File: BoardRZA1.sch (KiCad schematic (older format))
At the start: 151 parts, among them CON1 USB-MINI-B, CON2 USB-MINI-B, CON3 con-microSD, CON4 BARREL_JACK, J1 HR911105A, J2 SIL38, P1 CONN_5X2, SW1 RESET, SW2 NMI, SW3 SW0, SW4 SW1, U1 RZ-A1L, U2 OSC_4PIN, U3 OSC_4PIN, U4 N25QXXX, U5 AS4C16M16S, U6 BA3259HFP, U7 BU42xx, U8 KSZ8041MLL, X1 32.768k, X2 20MHz

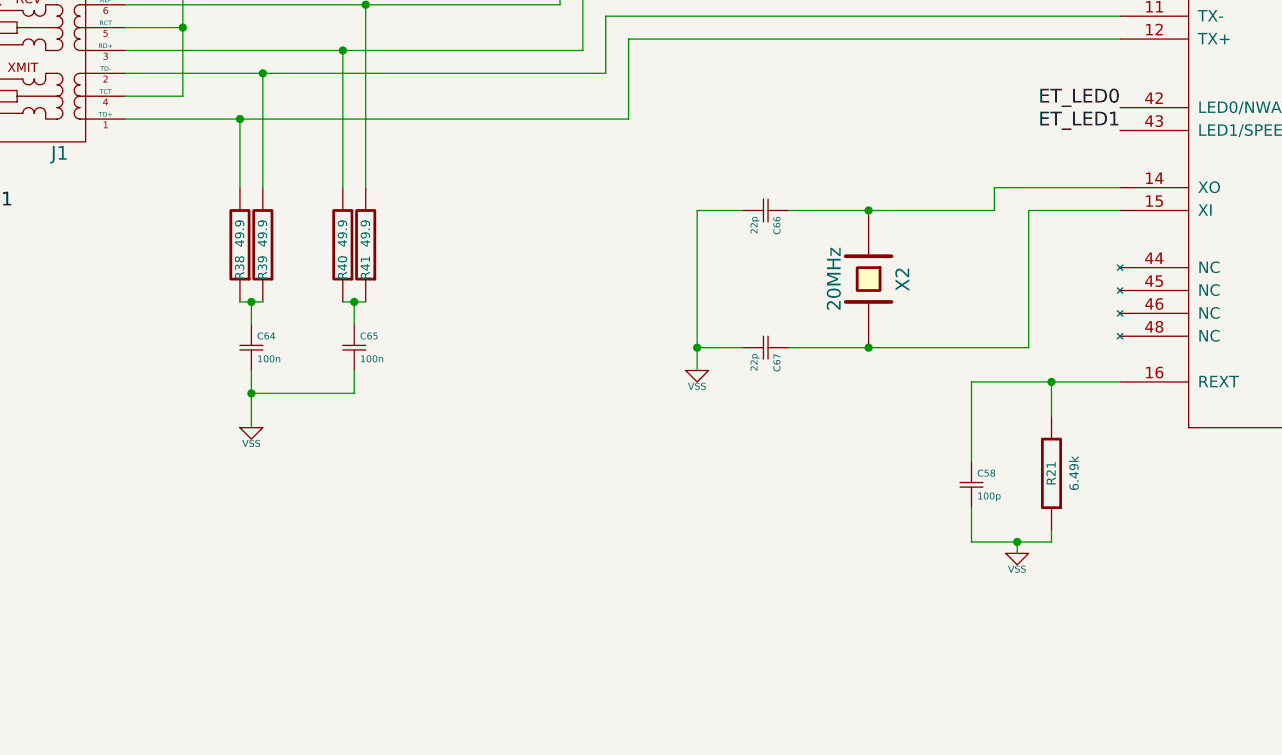
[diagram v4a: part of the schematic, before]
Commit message: Cambia XTAL 25MHz Phy por OSC 25MHz
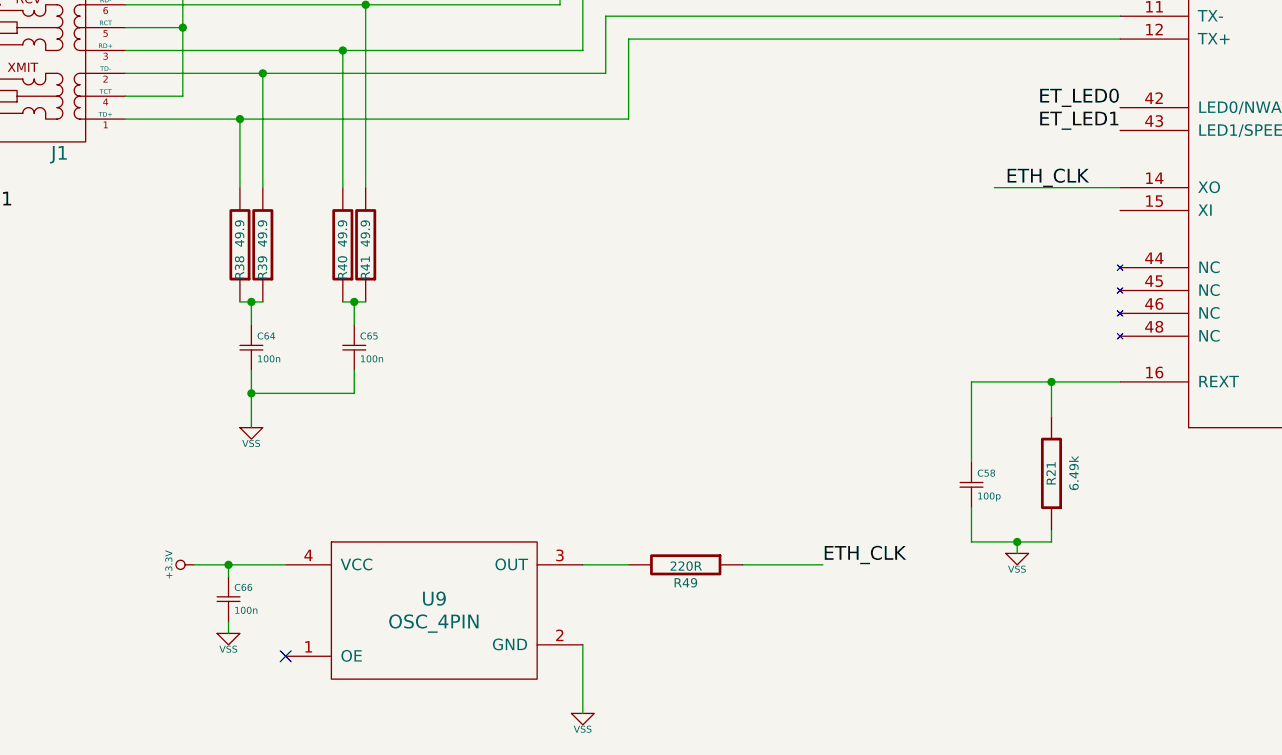
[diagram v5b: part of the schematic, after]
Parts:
- removed C67: 22p, SMD_Packages:SM0805, symbol Csmall
- removed X2: 20MHz, Crystals:Crystal_HC49-SD_SMD, symbol CRYSTAL
- added R49: 220R, SMD_Packages:SM0805, symbol R
- added U9: OSC_4PIN, OSC_4PIN:OSC_4PIN, symbol OSC_4PIN
- C66: value 22p -> 100n
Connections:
- net +3.3V: now also C66.1, U9.4 (VCC)
- net VSS: now also U9.2 (GND)
- net ETH_CLK: now reaches U8.14 (XO)
- net ETH_CLK: now also R49.1; no longer C66.1
- new net: R49.2, U9.3 (OUT)
- no-connect marks 13 -> 14
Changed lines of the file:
@@
 PHY_RESET
-$Comp
-L CRYSTAL X2
-U 1 1 5466F768
-P 22850 24400
-F 0 "X2" H 22850 24550 60  0000 C CNN
-F 1 "20MHz" H 22850 24250 60  0000 C CNN
-F 2 "Crystals:Crystal_HC49-SD_SMD" H 22850 24400 60  0001 C CNN
-F 3 "" H 22850 24400 60  0000 C CNN
-	1    22850 24400
-	0    1    1    0
-$EndComp
-$Comp
-L Csmall C67
-U 1 1 5466FA33
-P 22400 24700
-F 0 "C67" H 22425 24750 30  0000 L CNN
-F 1 "22p" H 22425 24650 30  0000 L CNN
-F 2 "SMD_Packages:SM0805" H 22400 24700 60  0001 C CNN
-F 3 "" H 22400 24700 60  0000 C CNN
-	1    22400 24700
-	0    1    1    0
-$EndComp
-$Comp
-L Csmall C66
-U 1 1 5466FE7E
-P 22400 24100
-F 0 "C66" H 22425 24150 30  0000 L CNN
-F 1 "22p" H 22425 24050 30  0000 L CNN
-F 2 "SMD_Packages:SM0805" H 22400 24100 60  0001 C CNN
-F 3 "" H 22400 24100 60  0000 C CNN
-	1    22400 24100
-	0    1    1    0
-$EndComp
-$Comp
-L VSS #PWR055
-U 1 1 54671C74
-P 22100 24800
-F 0 "#PWR055" H 22100 24800 30  0001 C CNN
-F 1 "VSS" H 22100 24730 30  0000 C CNN
-F 2 "" H 22100 24800 60  0000 C CNN
-F 3 "" H 22100 24800 60  0000 C CNN
-	1    22100 24800
-	1    0    0    -1
-$EndComp
 $Comp
 L INDUCTOR_SMALL L10
@@
 $EndComp
 $Comp
-L VSS #PWR056
+L VSS #PWR055
 U 1 1 5467CDAE
 P 20150 25050
-F 0 "#PWR056" H 20150 25050 30  0001 C CNN
+F 0 "#PWR055" H 20150 25050 30  0001 C CNN
 F 1 "VSS" H 20150 24980 30  0000 C CNN
 F 2 "" H 20150 25050 60  0000 C CNN
@@
 $EndComp
 $Comp
-L VSS #PWR057
+L VSS #PWR056
 U 1 1 5467DB95
 P 18250 24100
-F 0 "#PWR057" H 18250 24100 30  0001 C CNN
+F 0 "#PWR056" H 18250 24100 30  0001 C CNN
 F 1 "VSS" H 18250 24030 30  0000 C CNN
 F 2 "" H 18250 24100 60  0000 C CNN
@@
 $EndComp
 $Comp
-L VSS #PWR058
+L VSS #PWR057
 U 1 1 5467E4B1
 P 18050 22600
-F 0 "#PWR058" H 18050 22600 30  0001 C CNN
+F 0 "#PWR057" H 18050 22600 30  0001 C CNN
 F 1 "VSS" H 18050 22530 30  0000 C CNN
 F 2 "" H 18050 22600 60  0000 C CNN
@@
 $EndComp
 $Comp
-L VSS #PWR059
+L VSS #PWR058
 U 1 1 5467ECC7
 P 19950 23100
-F 0 "#PWR059" H 19950 23100 30  0001 C CNN
+F 0 "#PWR058" H 19950 23100 30  0001 C CNN
 F 1 "VSS" H 19950 23030 30  0000 C CNN
 F 2 "" H 19950 23100 60  0000 C CNN
@@
 $EndComp
 $Comp
-L +3.3V #PWR060
+L +3.3V #PWR059
 U 1 1 546866CA
 P 18600 21700
-F 0 "#PWR060" H 18600 21660 30  0001 C CNN
+F 0 "#PWR059" H 18600 21660 30  0001 C CNN
 F 1 "+3.3V" H 18600 21810 30  0000 C CNN
 F 2 "" H 18600 21700 60  0000 C CNN
@@
 	26250 22600 26850 22600
 Wire Wire Line
-	22500 24100 23400 24100
-Wire Wire Line
 	23950 24000 23400 24000
-Wire Wire Line
-	23400 24000 23400 24100
-Connection ~ 22850 24100
-Wire Wire Line
-	22500 24700 23550 24700
-Wire Wire Line
-	23550 24700 23550 24100
-Wire Wire Line
-	23550 24100 23950 24100
-Connection ~ 22850 24700
-Wire Wire Line
-	22300 24100 22100 24100
-Wire Wire Line
-	22100 24100 22100 24800
-Wire Wire Line
-	22100 24700 22300 24700
-Connection ~ 22100 24700
 Wire Wire Line
 	19600 23500 21700 23500
@@
 Connection ~ 18500 24100
 $Comp
-L VSS #PWR061
+L VSS #PWR060
 U 1 1 5468A27A
 P 18500 24750
-F 0 "#PWR061" H 18500 24750 30  0001 C CNN
+F 0 "#PWR060" H 18500 24750 30  0001 C CNN
 F 1 "VSS" H 18500 24680 30  0000 C CNN
 F 2 "" H 18500 24750 60  0000 C CNN
@@
 $EndComp
 $Comp
-L +3.3V #PWR062
+L +3.3V #PWR061
 U 1 1 5468A8E5
 P 18800 24650
-F 0 "#PWR062" H 18800 24610 30  0001 C CNN
+F 0 "#PWR061" H 18800 24610 30  0001 C CNN
 F 1 "+3.3V" H 18800 24760 30  0000 C CNN
 F 2 "" H 18800 24650 60  0000 C CNN
@@
 	18500 24650 18500 24750
 $Comp
-L VSS #PWR063
+L VSS #PWR062
 U 1 1 546806AB
 P 8350 12150
-F 0 "#PWR063" H 8350 12150 30  0001 C CNN
+F 0 "#PWR062" H 8350 12150 30  0001 C CNN
 F 1 "VSS" H 8350 12080 30  0000 C CNN
 F 2 "" H 8350 12150 60  0000 C CNN
@@
 	8350 11950 8100 11950
 $Comp
-L +3.3V #PWR064
+L +3.3V #PWR063
 U 1 1 54681794
 P 8200 8100
-F 0 "#PWR064" H 8200 8060 30  0001 C CNN
+F 0 "#PWR063" H 8200 8060 30  0001 C CNN
 F 1 "+3.3V" H 8200 8210 30  0000 C CNN
 F 2 "" H 8200 8100 60  0000 C CNN
@@
 $EndComp
 $Comp
-L +3.3V #PWR065
+L +3.3V #PWR064
 U 1 1 5468C052
 P 15250 3050
-F 0 "#PWR065" H 15250 3010 30  0001 C CNN
+F 0 "#PWR064" H 15250 3010 30  0001 C CNN
 F 1 "+3.3V" H 15250 3160 30  0000 C CNN
 F 2 "" H 15250 3050 60  0000 C CNN
@@
 $EndComp
 $Comp
-L +3.3V #PWR066
+L +3.3V #PWR065
 U 1 1 5468A3EB
 P 23550 2850
-F 0 "#PWR066" H 23550 2810 30  0001 C CNN
+F 0 "#PWR065" H 23550 2810 30  0001 C CNN
 F 1 "+3.3V" H 23550 2960 30  0000 C CNN
 F 2 "" H 23550 2850 60  0000 C CNN
@@
 	24150 2850 24400 2850
 $Comp
-L VSS #PWR067
+L VSS #PWR066
 U 1 1 5468ACC4
 P 25150 2850
-F 0 "#PWR067" H 25150 2850 30  0001 C CNN
+F 0 "#PWR066" H 25150 2850 30  0001 C CNN
 F 1 "VSS" H 25150 2780 30  0000 C CNN
 F 2 "" H 25150 2850 60  0000 C CNN
@@
 $EndComp
 $Comp
-L +3.3V #PWR068
+L +3.3V #PWR067
 U 1 1 5468CA07
 P 23550 3150
-F 0 "#PWR068" H 23550 3110 30  0001 C CNN
+F 0 "#PWR067" H 23550 3110 30  0001 C CNN
 F 1 "+3.3V" H 23550 3260 30  0000 C CNN
 F 2 "" H 23550 3150 60  0000 C CNN
@@
 	24150 3150 24400 3150
 $Comp
-L VSS #PWR069
+L VSS #PWR068
 U 1 1 5468CA0F
 P 25150 3150
-F 0 "#PWR069" H 25150 3150 30  0001 C CNN
+F 0 "#PWR068" H 25150 3150 30  0001 C CNN
 F 1 "VSS" H 25150 3080 30  0000 C CNN
 F 2 "" H 25150 3150 60  0000 C CNN
@@
 $EndComp
 $Comp
-L +3.3V #PWR070
+L +3.3V #PWR069
 U 1 1 54690CFD
 P 25050 3450
-F 0 "#PWR070" H 25050 3410 30  0001 C CNN
+F 0 "#PWR069" H 25050 3410 30  0001 C CNN
 F 1 "+3.3V" H 25050 3560 30  0000 C CNN
 F 2 "" H 25050 3450 60  0000 C CNN
@@
 $EndComp
 $Comp
-L +3.3V #PWR071
+L +3.3V #PWR070
 U 1 1 54691C17
 P 25050 3700
-F 0 "#PWR071" H 25050 3660 30  0001 C CNN
+F 0 "#PWR070" H 25050 3660 30  0001 C CNN
 F 1 "+3.3V" H 25050 3810 30  0000 C CNN
 F 2 "" H 25050 3700 60  0000 C CNN
@@
 $EndComp
 $Comp
-L +3.3V #PWR072
+L +3.3V #PWR071
 U 1 1 546923F5
 P 25050 3950
-F 0 "#PWR072" H 25050 3910 30  0001 C CNN
+F 0 "#PWR071" H 25050 3910 30  0001 C CNN
 F 1 "+3.3V" H 25050 4060 30  0000 C CNN
 F 2 "" H 25050 3950 60  0000 C CNN
@@
 $EndComp
 $Comp
-L +3.3V #PWR073
+L +3.3V #PWR072
 U 1 1 54692552
 P 25050 4200
-F 0 "#PWR073" H 25050 4160 30  0001 C CNN
+F 0 "#PWR072" H 25050 4160 30  0001 C CNN
 F 1 "+3.3V" H 25050 4310 30  0000 C CNN
 F 2 "" H 25050 4200 60  0000 C CNN
@@
 Wire Wire Line
 	23650 4200 23850 4200
+$Comp
+L OSC_4PIN U9
+U 1 1 546AB667
+P 20950 25850
+F 0 "U9" H 20950 25900 60  0000 C CNN
+F 1 "OSC_4PIN" H 20950 25800 60  0000 C CNN
+F 2 "OSC_4PIN:OSC_4PIN" H 20950 25900 60  0001 C CNN
+F 3 "" H 20950 25900 60  0000 C CNN
+	1    20950 25850
+	1    0    0    -1
+$EndComp
+$Comp
+L VSS #PWR073
+U 1 1 546AB66D
+P 21600 26300
+F 0 "#PWR073" H 21600 26300 30  0001 C CNN
+F 1 "VSS" H 21600 26230 30  0000 C CNN
+F 2 "" H 21600 26300 60  0000 C CNN
+F 3 "" H 21600 26300 60  0000 C CNN
+	1    21600 26300
+	1    0    0    -1
+$EndComp
+NoConn ~ 20300 26050
+$Comp
+L +3.3V #PWR074
+U 1 1 546AB674
+P 19900 25650
+F 0 "#PWR074" H 19900 25610 30  0001 C CNN
+F 1 "+3.3V" H 19900 25760 30  0000 C CNN
+F 2 "" H 19900 25650 60  0000 C CNN
+F 3 "" H 19900 25650 60  0000 C CNN
+	1    19900 25650
+	0    -1   -1   0
+$EndComp
+$Comp
+L Csmall C66
+U 1 1 546AB67A
+P 20050 25800
+F 0 "C66" H 20075 25850 30  0000 L CNN
+F 1 "100n" H 20075 25750 30  0000 L CNN
+F 2 "SMD_Packages:SM0805" H 20050 25800 60  0001 C CNN
+F 3 "" H 20050 25800 60  0000 C CNN
+	1    20050 25800
+	1    0    0    -1
+$EndComp
+$Comp
+L VSS #PWR075
+U 1 1 546AB680
+P 20050 25950
+F 0 "#PWR075" H 20050 25950 30  0001 C CNN
+F 1 "VSS" H 20050 25880 30  0000 C CNN
+F 2 "" H 20050 25950 60  0000 C CNN
+F 3 "" H 20050 25950 60  0000 C CNN
+	1    20050 25950
+	1    0    0    -1
+$EndComp
+$Comp
+L R R49
+U 1 1 546AB686
+P 22050 25650
+F 0 "R49" V 22130 25650 40  0000 C CNN
+F 1 "220R" V 22057 25651 40  0000 C CNN
+F 2 "SMD_Packages:SM0805" V 21980 25650 30  0001 C CNN
+F 3 "" H 22050 25650 30  0000 C CNN
+	1    22050 25650
+	0    1    1    0
+$EndComp
+Text Label 22650 25650 0    60   ~ 0
+ETH_CLK
+Wire Wire Line
+	21600 26300 21600 26000
+Wire Wire Line
+	19900 25650 20300 25650
+Wire Wire Line
+	20050 25650 20050 25700
+Connection ~ 20050 25650
+Wire Wire Line
+	20050 25950 20050 25900
+Wire Wire Line
+	21800 25650 21600 25650
+Wire Wire Line
+	22300 25650 22650 25650
+Text Label 23450 24000 0    60   ~ 0
+ETH_CLK
 $EndSCHEMATC

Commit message: USB-B CON2 -> USB-A CON2
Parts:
- removed CON2: USB-MINI-B, Connect:USB_MINI_B, symbol USB-MINI-B
- added CON2: USB-A-PCB, Connect:USB_A, symbol USB-A-PCB
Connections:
- net VSS: now also CON2.4 (GND)
- net at U1.167 (DM1): now also CON2.2 (D-)
- net at U1.168 (DP1): now also CON2.3 (D+)
- net +5v: now reaches U1.169 (VBUSIN1)
- net +5v: now also C47.1, C48.1, C49.1, CON4.1, U6.1 (Vcc), CON2.1 (VBUS)
- no-connect marks 14 -> 13
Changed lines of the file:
@@
 LIBS:hr911105a
 LIBS:sil40
+LIBS:usb-a-pcb
 LIBS:BoardRZA1-cache
 EELAYER 24 0
@@
 	1    0    0    -1
 $EndComp
-$Comp
-L USB-MINI-B CON2
-U 1 1 5457C33A
-P 31200 11900
-F 0 "CON2" H 30950 12350 60  0000 C CNN
-F 1 "USB-MINI-B" H 31150 11400 60  0000 C CNN
-F 2 "Connect:USB_MINI_B" H 31200 11900 60  0001 C CNN
-F 3 "" H 31200 11900 60  0000 C CNN
-	1    31200 11900
-	1    0    0    -1
-$EndComp
 NoConn ~ 30650 10900
-NoConn ~ 30650 12050
 $Comp
 L VSS #PWR031
@@
 	27950 11150 29850 11150
 Wire Wire Line
-	30650 11600 29950 11600
+	29950 11600 30750 11600
 Wire Wire Line
 	29950 11600 29950 11450
@@
 	29950 11450 27950 11450
 Wire Wire Line
-	27950 11550 29850 11550
-Wire Wire Line
-	29850 11550 29850 11900
-Wire Wire Line
-	29850 11900 30650 11900
-Wire Wire Line
-	30650 11750 29750 11750
-Wire Wire Line
-	29750 11750 29750 11650
-Wire Wire Line
-	29750 11650 27950 11650
-Wire Wire Line
 	30650 11050 30200 11050
 Wire Wire Line
 	30200 11050 30200 12550
 Wire Wire Line
-	30200 12200 30650 12200
+	30200 12200 30750 12200
 Wire Wire Line
 	31750 10450 32150 10450
 Wire Wire Line
-	32150 10450 32150 12550
-Wire Wire Line
-	32150 12200 31750 12200
-Wire Wire Line
-	31750 12050 32150 12050
-Connection ~ 32150 12050
-Wire Wire Line
-	31750 11750 32150 11750
-Connection ~ 32150 11750
-Wire Wire Line
-	32150 11600 31750 11600
-Connection ~ 32150 11600
-Wire Wire Line
-	31750 11050 32150 11050
+	32150 11050 31750 11050
 Connection ~ 32150 11050
 Wire Wire Line
-	31750 10900 32150 10900
+	32150 10900 31750 10900
 Connection ~ 32150 10900
 Wire Wire Line
@@
 Connection ~ 32150 10600
 Wire Wire Line
-	32150 12550 30200 12550
-Connection ~ 32150 12200
+	30200 12550 32150 12550
 Connection ~ 30200 12200
 Wire Wire Line
-	32300 11900 32150 11900
-Connection ~ 32150 11900
-Wire Wire Line
 	14700 8300 14700 8400
 Wire Wire Line
@@
 Text Label 23450 24000 0    60   ~ 0
 ETH_CLK
+$Comp
+L USB-A-PCB CON2
+U 1 1 546BEA89
+P 31150 11900
+F 0 "CON2" H 31150 12350 60  0000 C CNN
+F 1 "USB-A-PCB" H 31250 11400 60  0000 C CNN
+F 2 "Connect:USB_A" H 31150 11900 60  0001 C CNN
+F 3 "" H 31150 11900 60  0000 C CNN
+	1    31150 11900
+	1    0    0    -1
+$EndComp
+Wire Wire Line
+	32150 12550 32150 10450
+Wire Wire Line
+	32300 11900 32150 11900
+Connection ~ 32150 11900
+Wire Wire Line
+	27950 11650 29850 11650
+Wire Wire Line
+	29850 11650 29850 11800
+Wire Wire Line
+	29850 11800 30750 11800
+Wire Wire Line
+	27950 11550 29750 11550
+Wire Wire Line
+	29750 11550 29750 12000
+Wire Wire Line
+	29750 12000 30750 12000
+Text Label 14400 2450 0    60   ~ 0
++5v
+Text Label 30400 11600 0    60   ~ 0
++5v
 $EndSCHEMATC

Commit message: Add power from mini usb-b Prettify 3D
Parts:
- added D5, D6: MBRA210, Diodes_SMD:Diode-SMA_Standard, symbol DIODE
- P1: footprint Pin_Headers:Pin_Header_Straight_2x05 -> Connect:VASCH5x2
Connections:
- net +5v: now also D5.2 (K), D6.2 (K); no longer CON4.1
- net at CON1.1 (VBUS), U1.176 (VBUSIN0): now also D6.1 (A)
- new net: CON4.1, D5.1 (A)
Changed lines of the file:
@@
 F 0 "P1" H 30300 16050 60  0000 C CNN
 F 1 "CONN_5X2" V 30300 15750 50  0000 C CNN
-F 2 "Pin_Headers:Pin_Header_Straight_2x05" H 30300 15750 60  0001 C CNN
+F 2 "Connect:VASCH5x2" H 30300 15750 60  0001 C CNN
 F 3 "" H 30300 15750 60  0000 C CNN
 	1    30300 15750
@@
 	27950 12450 28650 12450
 Wire Wire Line
-	27950 11050 29750 11050
+	29750 11050 27950 11050
 Wire Wire Line
-	29750 11050 29750 10450
+	29750 10050 29750 11050
 Wire Wire Line
 	29750 10450 30650 10450
@@
 Connection ~ 14950 2300
 Wire Wire Line
-	14050 2450 15100 2450
-Wire Wire Line
 	15300 2450 15500 2450
 Wire Wire Line
@@
 Wire Wire Line
 	29750 12000 30750 12000
-Text Label 14400 2450 0    60   ~ 0
+Text Label 14950 2050 0    60   ~ 0
 +5v
 Text Label 30400 11600 0    60   ~ 0
 +5v
+Wire Wire Line
+	14650 2450 15100 2450
+$Comp
+L DIODE D5
+U 1 1 546D50B2
+P 14450 2450
+F 0 "D5" H 14450 2550 40  0000 C CNN
+F 1 "MBRA210" H 14450 2350 40  0000 C CNN
+F 2 "Diodes_SMD:Diode-SMA_Standard" H 14450 2450 60  0001 C CNN
+F 3 "" H 14450 2450 60  0000 C CNN
+	1    14450 2450
+	1    0    0    -1
+$EndComp
+Wire Wire Line
+	14250 2450 14050 2450
+$Comp
+L DIODE D6
+U 1 1 546D7C8E
+P 30450 10050
+F 0 "D6" H 30450 10150 40  0000 C CNN
+F 1 "MBRA210" H 30450 9950 40  0000 C CNN
+F 2 "Diodes_SMD:Diode-SMA_Standard" H 30450 10050 60  0001 C CNN
+F 3 "" H 30450 10050 60  0000 C CNN
+	1    30450 10050
+	1    0    0    -1
+$EndComp
+Wire Wire Line
+	30250 10050 29750 10050
+Connection ~ 29750 10450
+Wire Wire Line
+	30650 10050 31000 10050
+Text Label 31000 10050 0    60   ~ 0
++5v
 $EndSCHEMATC

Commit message: PHY OSC to XI fixed. Move some refs. Optional pulldown on TRST
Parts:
- added C? (x2): 10u, SMD_Packages:SM0805, symbol Csmall
- added D7: LED, LEDs:LED-0805, symbol LED
- added R50: 10k, SMD_Packages:SM0805, symbol R
- added R51: 220R, SMD_Packages:SM0805, symbol R
- U2: value OSC_4PIN -> 13MHz
- U3: value OSC_4PIN -> 48MHz
- U9: value OSC_4PIN -> 25MHz
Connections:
- net +3.3V: now also D7.2 (K)
- net ETH_CLK: now also U8.15 (XI); no longer U8.14 (XO)
- net JTAG_TRST: now also R50.2
- net PHY_RESET: now also U1.189 (P4_1/A18/VIO_HD/TIOC2B/ET_MDIO/RTS1)
- net USBAPVCC: now also C?.1
- net USBDPVCC: now also C?.1
- net VSS: now also C?.2, C?.2, R50.1, R51.1
- new net: D7.1 (A), R51.2
